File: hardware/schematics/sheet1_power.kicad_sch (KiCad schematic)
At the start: 40 parts, among them J1 2S_18650_7.4V_IN, J2 JST_XH_2S_BAL, J3 DC_IN_9-15V, Q1 AO3401A_PMOS, SW1 MASTER_SWITCH, U1 TP5100_2S_2A, U2 MP1584EN_3A, U3 AMS1117-3.3

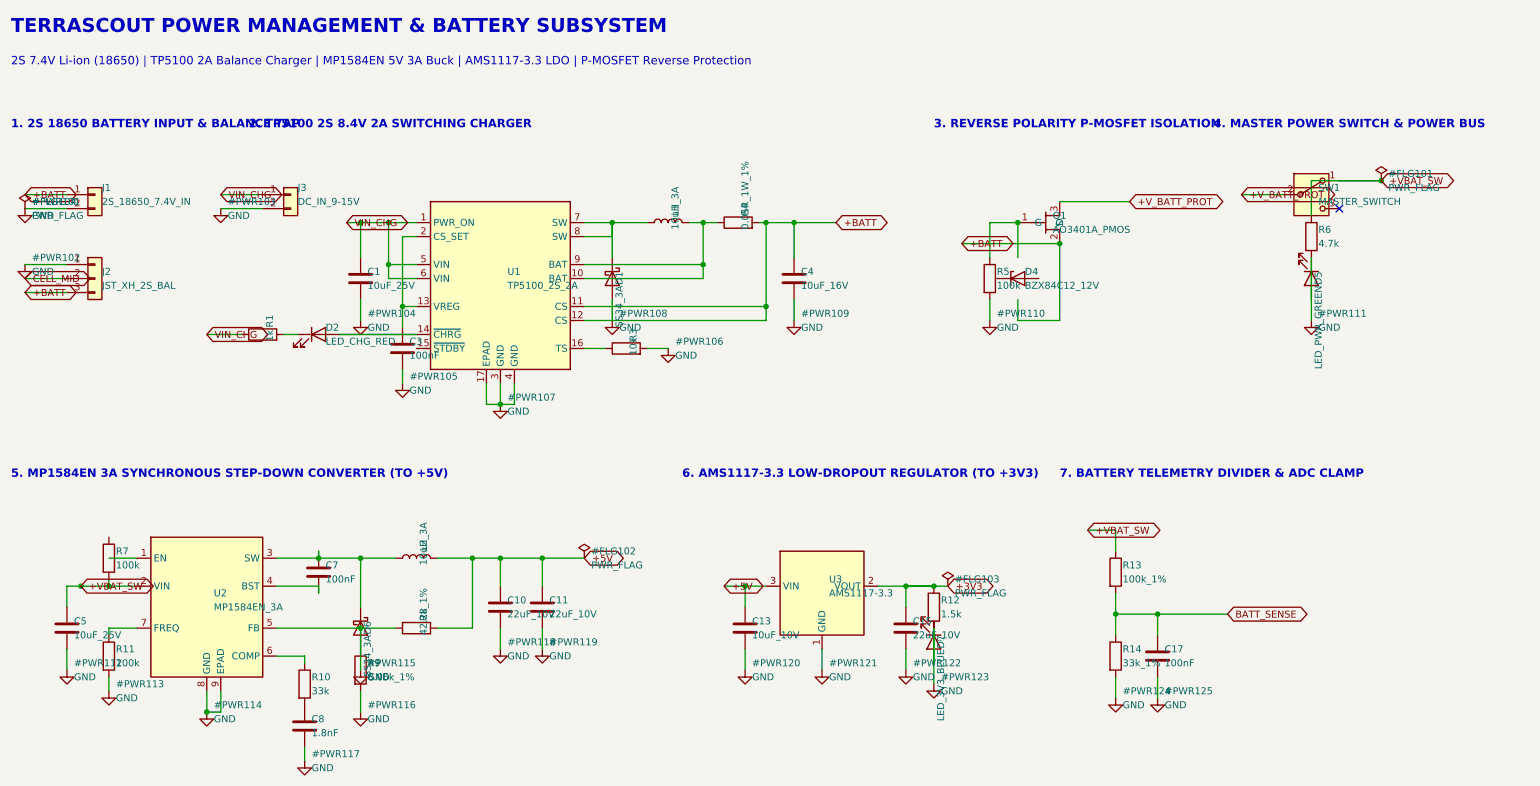
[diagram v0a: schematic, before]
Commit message: feat(cad): Update 3D-printable deck, motor brackets, and caster mount STL models
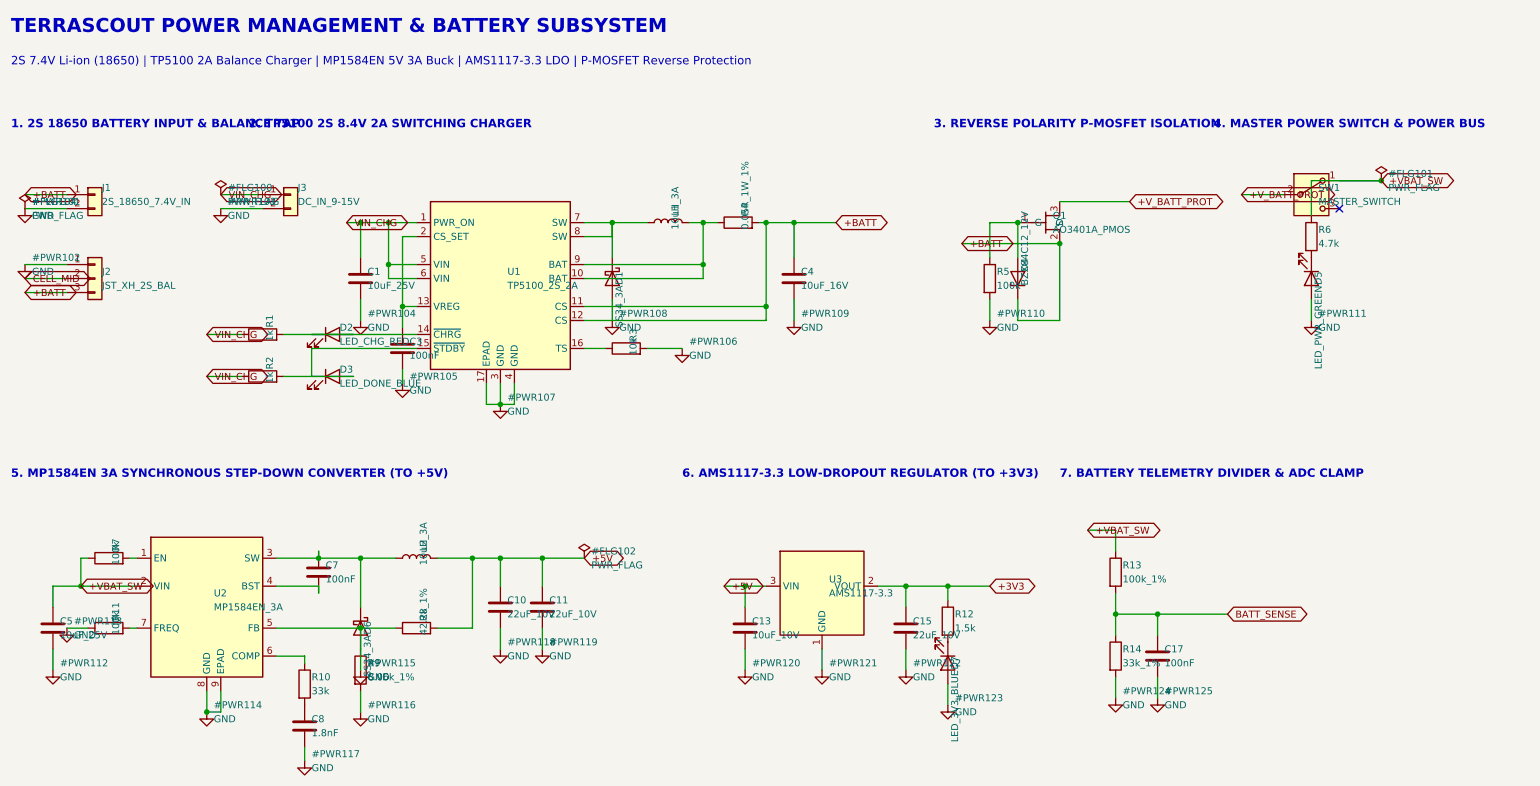
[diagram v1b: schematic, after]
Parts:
- added D3: LED_DONE_BLUE, LED_SMD:LED_0805_2012Metric, symbol Device:LED
- added R2: 1k, Resistor_SMD:R_0805_2012Metric, symbol Device:R
- D4: footprint Diode_SMD:D_SOT-23_ANK -> Diode_SMD:D_SOD-323
- J1: footprint TerminalBlock:TerminalBlock_bornier-2_P5.08mm -> TerminalBlock_Phoenix:TerminalBlock_Phoenix_MKDS-1,5-2-5.08_1x02_P5.08mm_Horizontal
- SW1: footprint Button_Switch_THT:SW_Slide_1P2T_SS-12D00G3 -> Button_Switch_THT:SW_DIP_SPSTx01_Slide_6.7x4.1mm_W7.62mm_P2.54mm_LowPro
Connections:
- net +BATT: now also D4.1 (K)
- net +VBAT_SW: now also R7.1; no longer R7.2
- net GND: now also R11.1; no longer D5.1 (K), R11.2, R12.2, R6.2
- net VIN_CHG: now also R2.1
- net at U2.1 (EN): now also R7.2
- net at U2.7 (FREQ): now also R11.2; no longer R11.1
- net at D2.2 (A), U1.14 (~{CHRG}): now also D2.1 (K), R1.2
- net at U1.15 (~{STDBY}): now also D3.1 (K)
- net at D7.1 (K): now also R12.2
- net at D4.2 (A): now also Q1.1 (G), R5.1
- new net: D5.1 (K), R6.2
- new net: D3.2 (A), R2.2
